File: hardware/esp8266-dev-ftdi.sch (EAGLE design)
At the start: 56 parts, among them CON1 USBMICRO-NO_CENTER-LONG_PADS

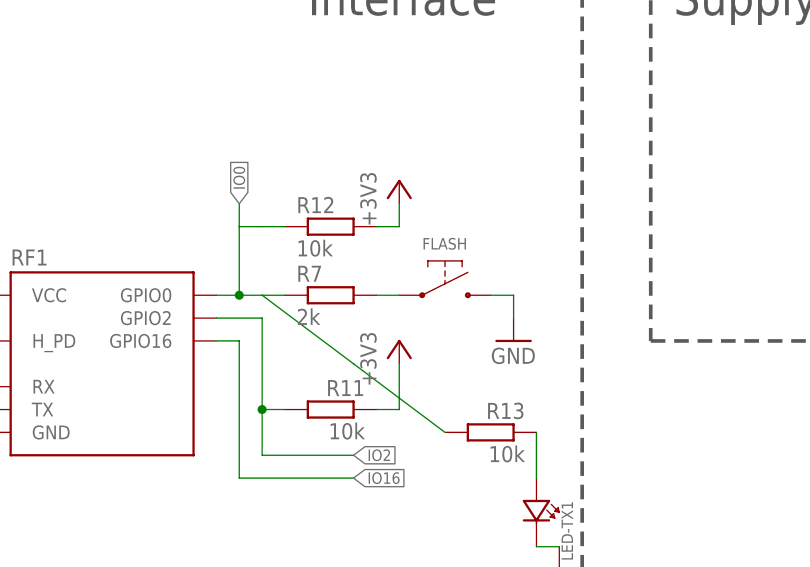
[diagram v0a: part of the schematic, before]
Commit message: basic layoutfor added components
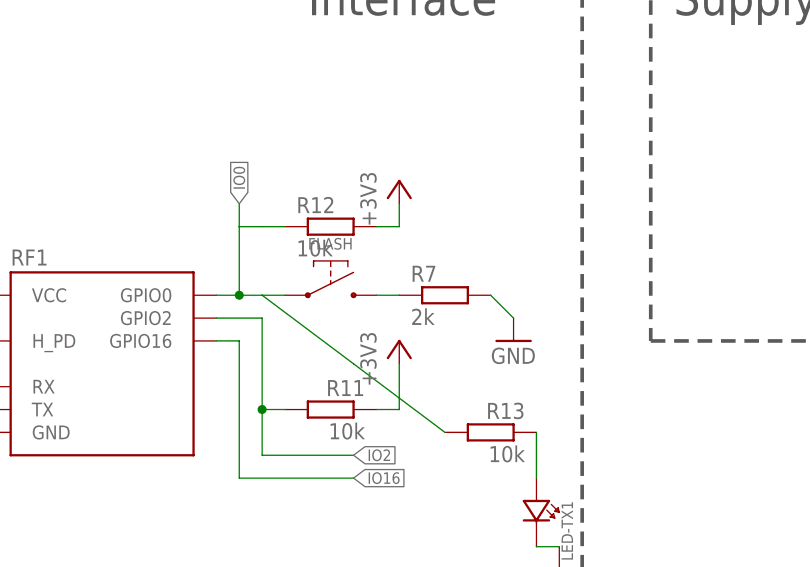
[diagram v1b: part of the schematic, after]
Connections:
- net GND: now also R7.2; no longer FLASH.P$2
- net IO0: now also FLASH.P$1; no longer R7.1
- net N$11: now also FLASH.P$2, R7.1; no longer FLASH.P$1, R7.2
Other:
- moved on the sheet: FLASH, R7
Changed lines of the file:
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@@
 <instance part="C7" gate="G$1" x="185.42" y="-40.64" rot="R180"/>
 <instance part="C8" gate="G$1" x="210.82" y="-40.64" rot="MR180"/>
-<instance part="FLASH" gate="S$1" x="119.38" y="-58.42"/>
+<instance part="FLASH" gate="S$1" x="106.68" y="-58.42"/>
 <instance part="RF1" gate="G$1" x="81.28" y="-66.04"/>
 <instance part="+3V7" gate="G$1" x="66.04" y="-53.34"/>
@@
 <instance part="R6" gate="G$1" x="48.26" y="-30.48" rot="MR0"/>
 <instance part="+3V8" gate="G$1" x="40.64" y="-25.4"/>
-<instance part="R7" gate="G$1" x="106.68" y="-58.42"/>
+<instance part="R7" gate="G$1" x="119.38" y="-58.42"/>
 <instance part="GND13" gate="1" x="127" y="-63.5"/>
 <instance part="U$2" gate="G$1" x="167.64" y="12.7" rot="R180"/>
@@
 </segment>
 <segment>
-<pinref part="FLASH" gate="S$1" pin="P$2"/>
 <pinref part="GND13" gate="1" pin="GND"/>
-<wire x1="127" y1="-60.96" x2="127" y2="-58.42" width="0.1524" layer="91"/>
-<wire x1="127" y1="-58.42" x2="124.46" y2="-58.42" width="0.1524" layer="91"/>
+<wire x1="127" y1="-60.96" x2="124.46" y2="-58.42" width="0.1524" layer="91"/>
+<pinref part="R7" gate="G$1" pin="2"/>
 </segment>
 <segment>
@@
 </segment>
 </net>
-<net name="N$11" class="0">
-<segment>
-<pinref part="R7" gate="G$1" pin="2"/>
-<pinref part="FLASH" gate="S$1" pin="P$1"/>
-<wire x1="114.3" y1="-58.42" x2="111.76" y2="-58.42" width="0.1524" layer="91"/>
-</segment>
-</net>
 <net name="IO2" class="0">
 <segment>
@@
 <segment>
 <pinref part="RF1" gate="G$1" pin="GPIO0"/>
-<pinref part="R7" gate="G$1" pin="1"/>
-<wire x1="101.6" y1="-58.42" x2="99.06" y2="-58.42" width="0.1524" layer="91"/>
 <wire x1="99.06" y1="-58.42" x2="96.52" y2="-58.42" width="0.1524" layer="91"/>
 <wire x1="96.52" y1="-58.42" x2="93.98" y2="-58.42" width="0.1524" layer="91"/>
@@
 <wire x1="99.06" y1="-58.42" x2="109.22" y2="-66.04" width="0.1524" layer="91"/>
 <wire x1="109.22" y1="-66.04" x2="119.38" y2="-73.66" width="0.1524" layer="91"/>
+<pinref part="FLASH" gate="S$1" pin="P$1"/>
+<wire x1="101.6" y1="-58.42" x2="99.06" y2="-58.42" width="0.1524" layer="91"/>
 </segment>
 <segment>
@@
 </segment>
 </net>
+<net name="N$11" class="0">
+<segment>
+<pinref part="R7" gate="G$1" pin="1"/>
+<pinref part="FLASH" gate="S$1" pin="P$2"/>
+<wire x1="111.76" y1="-58.42" x2="114.3" y2="-58.42" width="0.1524" layer="91"/>
+</segment>
+</net>

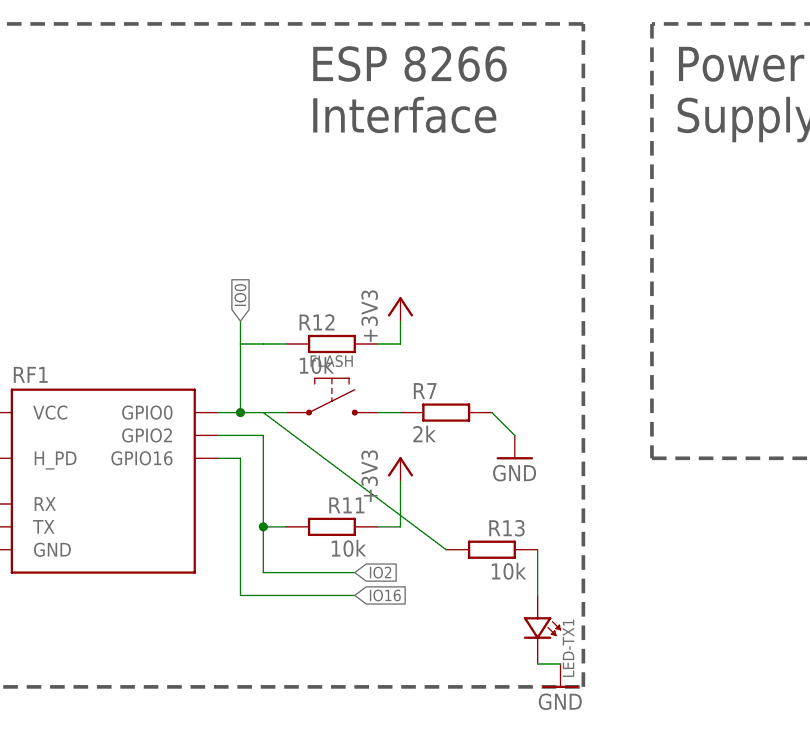
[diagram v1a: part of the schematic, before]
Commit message: cleaned up schematic
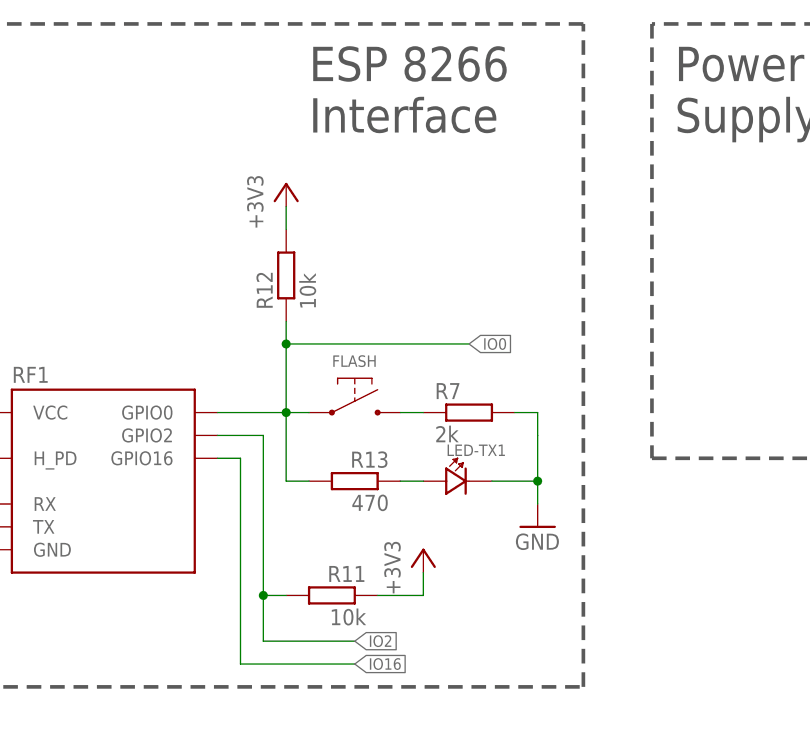
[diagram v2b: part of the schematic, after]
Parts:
- R13: value 10k -> 470
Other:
- moved on the sheet: FLASH, LED-TX1, R11, R12, R13, R7
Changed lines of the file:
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@@
 <part name="R12" library="p.peter-rcl" deviceset="R-EU_" device="R0805" value="10k"/>
 <part name="+3V9" library="supply1" deviceset="+3V3" device=""/>
-<part name="R13" library="p.peter-rcl" deviceset="R-EU_" device="R0805" value="10k"/>
+<part name="R13" library="p.peter-rcl" deviceset="R-EU_" device="R0805" value="470"/>
 <part name="LED-TX1" library="p.peter-leds" deviceset="LED" device="0805"/>
-<part name="GND25" library="supply1" deviceset="GND" device=""/>
 </parts>
 <sheets>
@@
 <instance part="C7" gate="G$1" x="185.42" y="-40.64" rot="R180"/>
 <instance part="C8" gate="G$1" x="210.82" y="-40.64" rot="MR180"/>
-<instance part="FLASH" gate="S$1" x="106.68" y="-58.42"/>
+<instance part="FLASH" gate="S$1" x="109.22" y="-58.42"/>
 <instance part="RF1" gate="G$1" x="81.28" y="-66.04"/>
 <instance part="+3V7" gate="G$1" x="66.04" y="-53.34"/>
@@
 <instance part="R6" gate="G$1" x="48.26" y="-30.48" rot="MR0"/>
 <instance part="+3V8" gate="G$1" x="40.64" y="-25.4"/>
-<instance part="R7" gate="G$1" x="119.38" y="-58.42"/>
-<instance part="GND13" gate="1" x="127" y="-63.5"/>
+<instance part="R7" gate="G$1" x="121.92" y="-58.42"/>
+<instance part="GND13" gate="1" x="129.54" y="-71.12"/>
 <instance part="U$2" gate="G$1" x="167.64" y="12.7" rot="R180"/>
 <instance part="GND15" gate="1" x="160.02" y="2.54"/>
@@
 <instance part="+3V5" gate="G$1" x="215.9" y="58.42"/>
 <instance part="GND24" gate="1" x="220.98" y="35.56"/>
-<instance part="R11" gate="G$1" x="106.68" y="-71.12" rot="MR0"/>
-<instance part="+3V1" gate="G$1" x="114.3" y="-63.5"/>
+<instance part="R11" gate="G$1" x="106.68" y="-78.74" rot="MR0"/>
+<instance part="+3V1" gate="G$1" x="116.84" y="-73.66"/>
 <instance part="P+6" gate="1" x="68.58" y="78.74" smashed="yes">
 <attribute name="VALUE" x="68.58" y="78.74" size="1.778" layer="96" rot="R90"/>
@@
 <instance part="3V3" gate="G$1" x="73.66" y="71.12"/>
 <instance part="GND" gate="G$1" x="78.74" y="71.12"/>
-<instance part="R12" gate="G$1" x="106.68" y="-50.8"/>
-<instance part="+3V9" gate="G$1" x="114.3" y="-45.72"/>
-<instance part="R13" gate="G$1" x="124.46" y="-73.66" rot="MR0"/>
-<instance part="LED-TX1" gate="G$1" x="129.54" y="-81.28" rot="R270"/>
-<instance part="GND25" gate="1" x="132.08" y="-88.9"/>
+<instance part="R12" gate="G$1" x="101.6" y="-43.18" rot="R90"/>
+<instance part="+3V9" gate="G$1" x="101.6" y="-33.02"/>
+<instance part="R13" gate="G$1" x="109.22" y="-66.04" rot="MR0"/>
+<instance part="LED-TX1" gate="G$1" x="119.38" y="-66.04"/>
 </instances>
 <busses>
@@
 <segment>
 <pinref part="GND13" gate="1" pin="GND"/>
-<wire x1="127" y1="-60.96" x2="124.46" y2="-58.42" width="0.1524" layer="91"/>
+<wire x1="129.54" y1="-68.58" x2="129.54" y2="-66.04" width="0.1524" layer="91"/>
+<wire x1="129.54" y1="-66.04" x2="129.54" y2="-60.96" width="0.1524" layer="91"/>
+<wire x1="129.54" y1="-60.96" x2="129.54" y2="-58.42" width="0.1524" layer="91"/>
+<wire x1="129.54" y1="-58.42" x2="127" y2="-58.42" width="0.1524" layer="91"/>
 <pinref part="R7" gate="G$1" pin="2"/>
+<pinref part="LED-TX1" gate="G$1" pin="C"/>
+<wire x1="124.46" y1="-66.04" x2="129.54" y2="-66.04" width="0.1524" layer="91"/>
+<junction x="129.54" y="-66.04"/>
 </segment>
 <segment>
@@
 <wire x1="78.74" y1="76.2" x2="78.74" y2="73.66" width="0.1524" layer="91"/>
 <pinref part="GND" gate="G$1" pin="TP"/>
-</segment>
-<segment>
-<pinref part="LED-TX1" gate="G$1" pin="C"/>
-<pinref part="GND25" gate="1" pin="GND"/>
-<wire x1="132.08" y1="-86.36" x2="129.54" y2="-86.36" width="0.1524" layer="91"/>
 </segment>
 </net>
@@
 <pinref part="R11" gate="G$1" pin="1"/>
 <pinref part="+3V1" gate="G$1" pin="+3V3"/>
-<wire x1="111.76" y1="-71.12" x2="114.3" y2="-71.12" width="0.1524" layer="91"/>
-<wire x1="114.3" y1="-71.12" x2="114.3" y2="-66.04" width="0.1524" layer="91"/>
+<wire x1="111.76" y1="-78.74" x2="116.84" y2="-78.74" width="0.1524" layer="91"/>
+<wire x1="116.84" y1="-78.74" x2="116.84" y2="-76.2" width="0.1524" layer="91"/>
 </segment>
 <segment>
@@
 <pinref part="R12" gate="G$1" pin="2"/>
 <pinref part="+3V9" gate="G$1" pin="+3V3"/>
-<wire x1="111.76" y1="-50.8" x2="114.3" y2="-50.8" width="0.1524" layer="91"/>
-<wire x1="114.3" y1="-50.8" x2="114.3" y2="-48.26" width="0.1524" layer="91"/>
+<wire x1="101.6" y1="-38.1" x2="101.6" y2="-35.56" width="0.1524" layer="91"/>
 </segment>
 </net>
@@
 <pinref part="RF1" gate="G$1" pin="GPIO2"/>
 <wire x1="93.98" y1="-60.96" x2="99.06" y2="-60.96" width="0.1524" layer="91"/>
-<wire x1="99.06" y1="-60.96" x2="99.06" y2="-71.12" width="0.1524" layer="91"/>
-<wire x1="99.06" y1="-71.12" x2="99.06" y2="-76.2" width="0.1524" layer="91"/>
-<wire x1="99.06" y1="-76.2" x2="109.22" y2="-76.2" width="0.1524" layer="91"/>
-<label x="109.22" y="-76.2" size="1.27" layer="95" xref="yes"/>
+<wire x1="99.06" y1="-60.96" x2="99.06" y2="-78.74" width="0.1524" layer="91"/>
+<wire x1="99.06" y1="-78.74" x2="99.06" y2="-83.82" width="0.1524" layer="91"/>
+<wire x1="99.06" y1="-83.82" x2="109.22" y2="-83.82" width="0.1524" layer="91"/>
+<label x="109.22" y="-83.82" size="1.27" layer="95" xref="yes"/>
 <pinref part="R11" gate="G$1" pin="2"/>
-<wire x1="101.6" y1="-71.12" x2="99.06" y2="-71.12" width="0.1524" layer="91"/>
-<junction x="99.06" y="-71.12"/>
+<wire x1="101.6" y1="-78.74" x2="99.06" y2="-78.74" width="0.1524" layer="91"/>
+<junction x="99.06" y="-78.74"/>
 </segment>
 <segment>
@@
 <pinref part="RF1" gate="G$1" pin="GPIO16"/>
 <wire x1="93.98" y1="-63.5" x2="96.52" y2="-63.5" width="0.1524" layer="91"/>
-<wire x1="96.52" y1="-63.5" x2="96.52" y2="-78.74" width="0.1524" layer="91"/>
-<wire x1="96.52" y1="-78.74" x2="109.22" y2="-78.74" width="0.1524" layer="91"/>
-<label x="109.22" y="-78.74" size="1.27" layer="95" xref="yes"/>
+<wire x1="96.52" y1="-63.5" x2="96.52" y2="-86.36" width="0.1524" layer="91"/>
+<wire x1="96.52" y1="-86.36" x2="109.22" y2="-86.36" width="0.1524" layer="91"/>
+<label x="109.22" y="-86.36" size="1.27" layer="95" xref="yes"/>
 </segment>
 <segment>
@@
 <segment>
 <pinref part="RF1" gate="G$1" pin="GPIO0"/>
-<wire x1="99.06" y1="-58.42" x2="96.52" y2="-58.42" width="0.1524" layer="91"/>
-<wire x1="96.52" y1="-58.42" x2="93.98" y2="-58.42" width="0.1524" layer="91"/>
-<wire x1="96.52" y1="-58.42" x2="96.52" y2="-50.8" width="0.1524" layer="91"/>
-<junction x="96.52" y="-58.42"/>
-<label x="96.52" y="-48.26" size="1.27" layer="95" rot="R90" xref="yes"/>
+<wire x1="101.6" y1="-58.42" x2="93.98" y2="-58.42" width="0.1524" layer="91"/>
+<wire x1="101.6" y1="-58.42" x2="101.6" y2="-50.8" width="0.1524" layer="91"/>
+<junction x="101.6" y="-58.42"/>
+<label x="121.92" y="-50.8" size="1.27" layer="95" xref="yes"/>
 <pinref part="R12" gate="G$1" pin="1"/>
-<wire x1="96.52" y1="-50.8" x2="96.52" y2="-48.26" width="0.1524" layer="91"/>
-<wire x1="101.6" y1="-50.8" x2="99.06" y2="-50.8" width="0.1524" layer="91"/>
-<wire x1="99.06" y1="-50.8" x2="96.52" y2="-50.8" width="0.1524" layer="91"/>
+<wire x1="101.6" y1="-50.8" x2="121.92" y2="-50.8" width="0.1524" layer="91"/>
+<wire x1="101.6" y1="-48.26" x2="101.6" y2="-50.8" width="0.1524" layer="91"/>
+<pinref part="FLASH" gate="S$1" pin="P$1"/>
+<wire x1="104.14" y1="-58.42" x2="101.6" y2="-58.42" width="0.1524" layer="91"/>
+<junction x="101.6" y="-50.8"/>
 <pinref part="R13" gate="G$1" pin="2"/>
-<wire x1="99.06" y1="-58.42" x2="109.22" y2="-66.04" width="0.1524" layer="91"/>
-<wire x1="109.22" y1="-66.04" x2="119.38" y2="-73.66" width="0.1524" layer="91"/>
-<pinref part="FLASH" gate="S$1" pin="P$1"/>
-<wire x1="101.6" y1="-58.42" x2="99.06" y2="-58.42" width="0.1524" layer="91"/>
+<wire x1="104.14" y1="-66.04" x2="101.6" y2="-66.04" width="0.1524" layer="91"/>
+<wire x1="101.6" y1="-66.04" x2="101.6" y2="-58.42" width="0.1524" layer="91"/>
 </segment>
 <segment>
@@
 <pinref part="R13" gate="G$1" pin="1"/>
 <pinref part="LED-TX1" gate="G$1" pin="A"/>
-<wire x1="129.54" y1="-78.74" x2="129.54" y2="-73.66" width="0.1524" layer="91"/>
+<wire x1="116.84" y1="-66.04" x2="114.3" y2="-66.04" width="0.1524" layer="91"/>
 </segment>
 </net>
@@
 <pinref part="R7" gate="G$1" pin="1"/>
 <pinref part="FLASH" gate="S$1" pin="P$2"/>
-<wire x1="111.76" y1="-58.42" x2="114.3" y2="-58.42" width="0.1524" layer="91"/>
-</segment>
-</net>
+<wire x1="114.3" y1="-58.42" x2="116.84" y2="-58.42" width="0.1524" layer="91"/>
+</segment>
+</net>

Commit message: minor cleanup
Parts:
- R13: value 470 -> 540
- R5: value 150 -> 540
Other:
- note added: "Do the WS2812b need caps?"
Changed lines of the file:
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@@
 <part name="GND11" library="supply1" deviceset="GND" device=""/>
 <part name="+3V3" library="supply1" deviceset="+3V3" device=""/>
-<part name="R5" library="p.peter-rcl" deviceset="R-EU_" device="R0805" value="150"/>
+<part name="R5" library="p.peter-rcl" deviceset="R-EU_" device="R0805" value="540"/>
 <part name="P+5" library="supply1" deviceset="+5V" device=""/>
 <part name="C7" library="p.peter-rcl" deviceset="C-EU" device="C0805" value="10u"/>
@@
 <part name="R12" library="p.peter-rcl" deviceset="R-EU_" device="R0805" value="10k"/>
 <part name="+3V9" library="supply1" deviceset="+3V3" device=""/>
-<part name="R13" library="p.peter-rcl" deviceset="R-EU_" device="R0805" value="470"/>
+<part name="R13" library="p.peter-rcl" deviceset="R-EU_" device="R0805" value="540"/>
 <part name="LED-TX1" library="p.peter-leds" deviceset="LED" device="0805"/>
 </parts>
@@
 v0.1 (8e144a9ffe)
 </text>
+<text x="86.36" y="83.82" size="5.08" layer="94">Do the WS2812b need caps?</text>
 </plain>
 <instances>
